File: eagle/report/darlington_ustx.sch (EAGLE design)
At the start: 2 parts

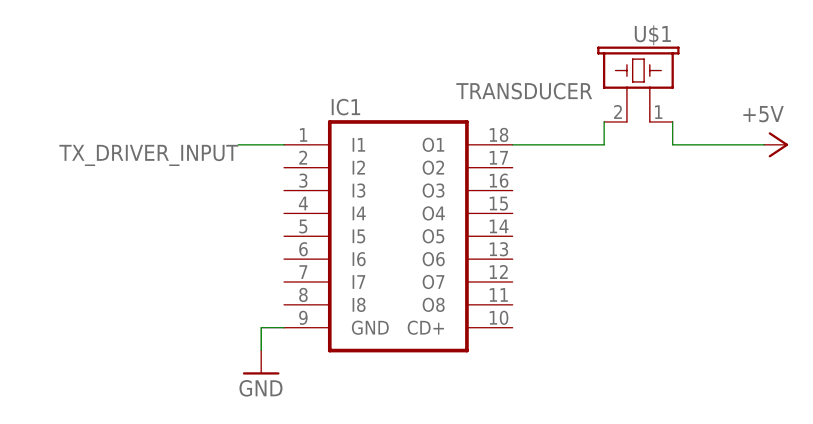
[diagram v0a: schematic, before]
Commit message: Tweaked various bits of design and implementation. Reduced font size on all diagrams and adjusted diagrams accordingly.
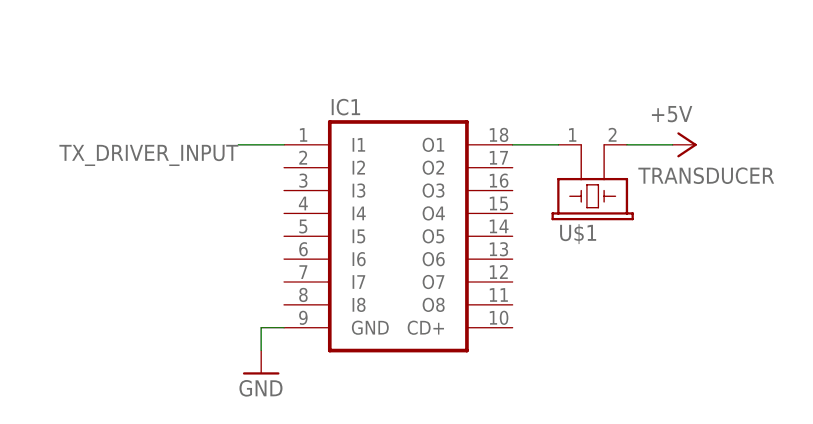
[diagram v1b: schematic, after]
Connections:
- net +5V: now also U$1.2; no longer U$1.1
- net N$1: now also U$1.1; no longer U$1.2
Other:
- moved on the sheet: U$1
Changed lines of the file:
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@@
 <?xml version="1.0" encoding="utf-8"?>
 <!DOCTYPE eagle SYSTEM "eagle.dtd">
-<eagle version="6.3">
+<eagle version="6.4">
 <drawing>
 <settings>
@@
 <instances>
 <instance part="IC1" gate="G$1" x="45.72" y="50.8"/>
-<instance part="U$1" gate="G$1" x="73.66" y="66.04" rot="MR0"/>
-<instance part="P+1" gate="1" x="88.9" y="60.96" rot="R270"/>
+<instance part="U$1" gate="G$1" x="66.04" y="58.42" rot="MR180"/>
+<instance part="P+1" gate="1" x="78.74" y="60.96" rot="R270"/>
 <instance part="GND1" gate="1" x="30.48" y="35.56"/>
 </instances>
@@
 </busses>
 <nets>
-<net name="N$1" class="0">
-<segment>
-<pinref part="IC1" gate="G$1" pin="O1"/>
-<wire x1="58.42" y1="60.96" x2="68.58" y2="60.96" width="0.1524" layer="91"/>
-<pinref part="U$1" gate="G$1" pin="2"/>
-<wire x1="68.58" y1="60.96" x2="68.58" y2="63.5" width="0.1524" layer="91"/>
-</segment>
-</net>
-<net name="+5V" class="0">
-<segment>
-<pinref part="U$1" gate="G$1" pin="1"/>
-<wire x1="76.2" y1="63.5" x2="76.2" y2="60.96" width="0.1524" layer="91"/>
-<pinref part="P+1" gate="1" pin="+5V"/>
-<wire x1="76.2" y1="60.96" x2="86.36" y2="60.96" width="0.1524" layer="91"/>
-</segment>
-</net>
 <net name="GND" class="0">
 <segment>
@@
 </segment>
 </net>
+<net name="+5V" class="0">
+<segment>
+<pinref part="U$1" gate="G$1" pin="2"/>
+<pinref part="P+1" gate="1" pin="+5V"/>
+<wire x1="76.2" y1="60.96" x2="71.12" y2="60.96" width="0.1524" layer="91"/>
+</segment>
+</net>
+<net name="N$1" class="0">
+<segment>
+<pinref part="IC1" gate="G$1" pin="O1"/>
+<pinref part="U$1" gate="G$1" pin="1"/>
+<wire x1="63.5" y1="60.96" x2="58.42" y2="60.96" width="0.1524" layer="91"/>
+</segment>
+</net>
